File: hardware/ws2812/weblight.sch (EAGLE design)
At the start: 16 parts, among them U1 ATtiny85-20SU

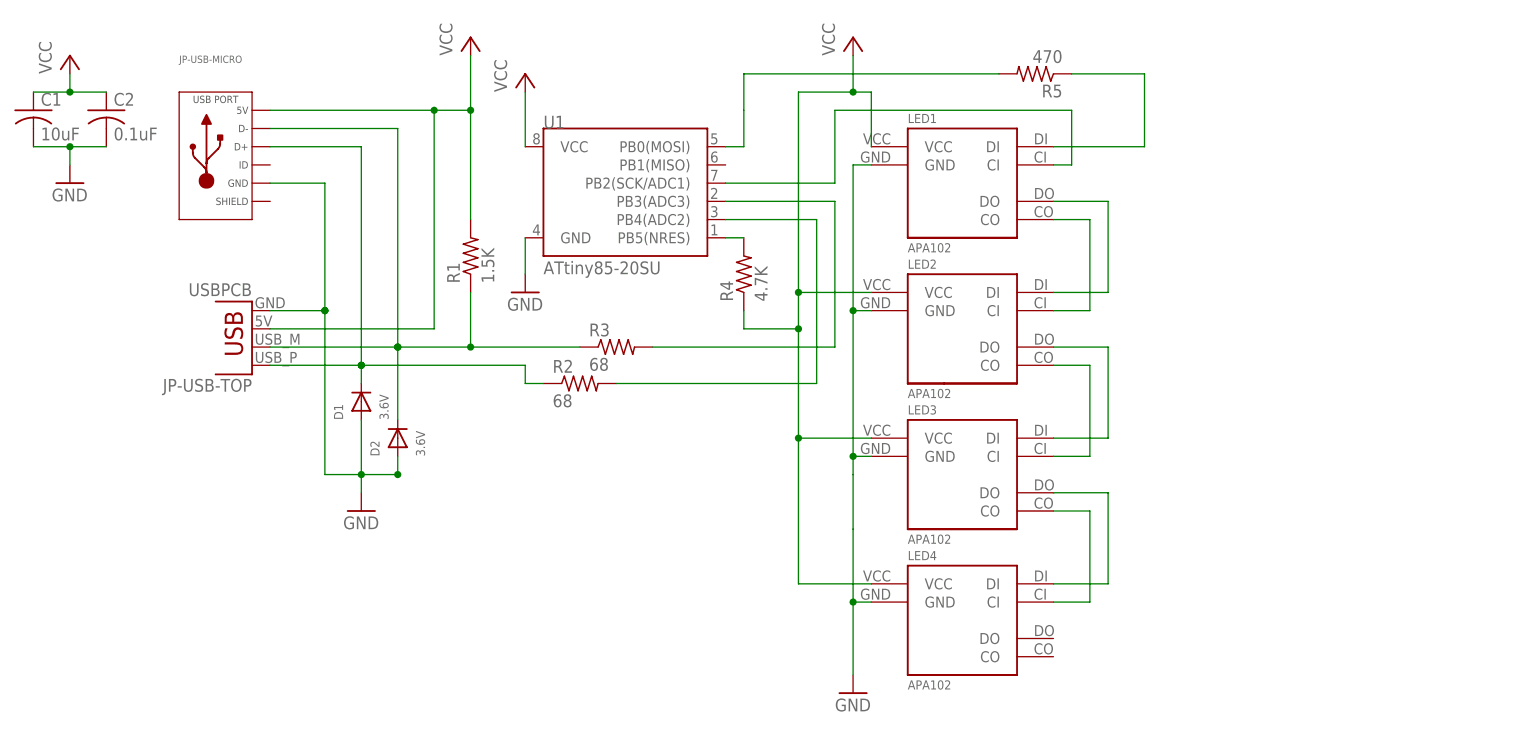
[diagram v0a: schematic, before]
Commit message: Separate LED type and adopt new board versioning scheme
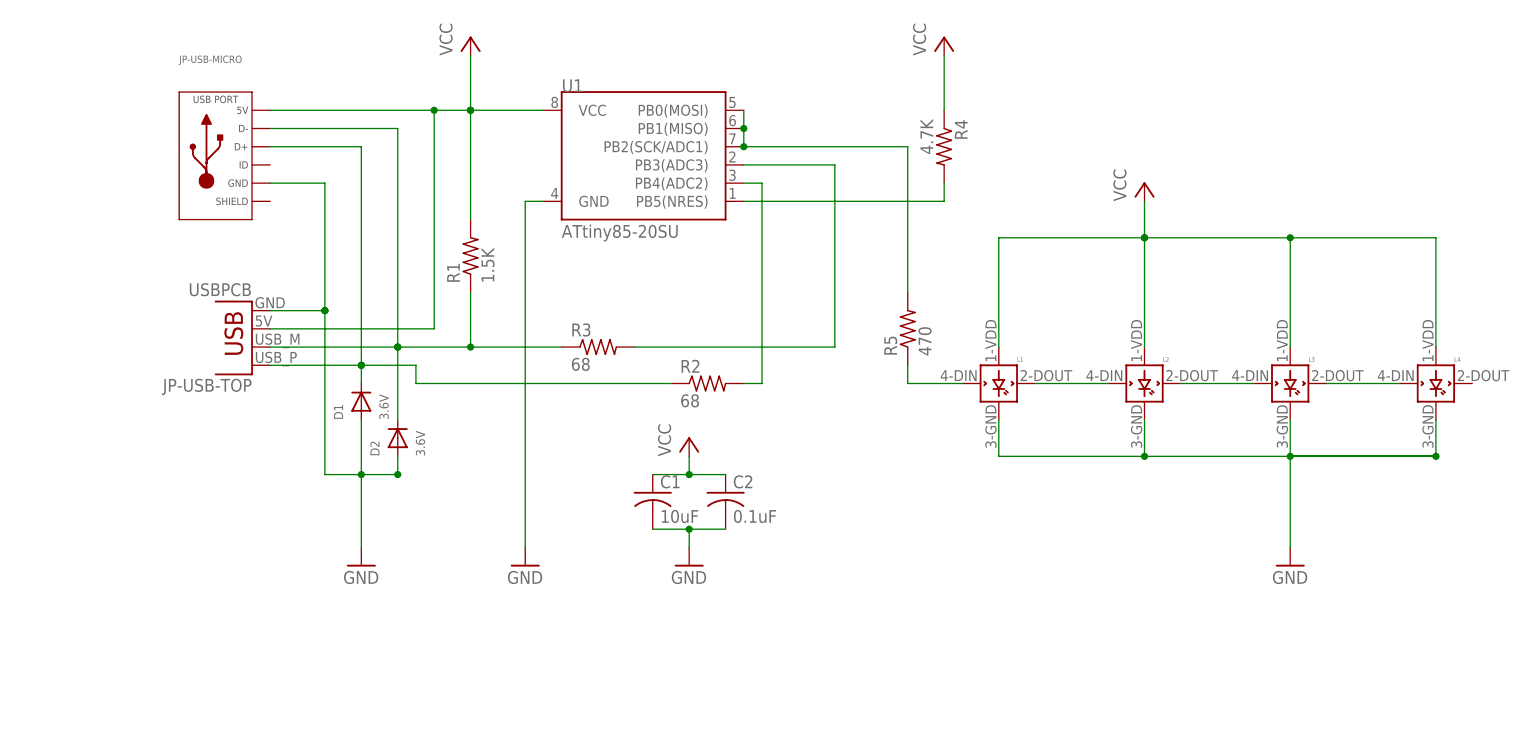
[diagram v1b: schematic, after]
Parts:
- removed LED1, LED2, LED3, LED4: APA102, weblight:APA102
- added L1, L2, L3, L4: WS2812B, weblight:WS2812B
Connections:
- removed net CLK_1: LED1.CI, U1.PB2(SCK/ADC1)
- removed net CLK_2: LED1.CO, LED2.CI
- removed net CLK_3: LED2.CO, LED3.CI
- removed net CLK_4: LED3.CO, LED4.CI
- net DIN_1: now also L1.DIN; no longer LED1.DI
- net DIN_2: now also L1.DOUT, L2.DIN; no longer LED1.DO, LED2.DI
- net DIN_3: now also L2.DOUT, L3.DIN; no longer LED2.DO, LED3.DI
- net DIN_4: now also L3.DOUT, L4.DIN; no longer LED3.DO, LED4.DI
- net DIN_RAW: now also U1.PB1(MISO), U1.PB2(SCK/ADC1)
- net GND: now also L1.GND, L2.GND, L3.GND, L4.GND; no longer LED1.GND, LED2.GND, LED3.GND, LED4.GND
- net VCC: now also L1.VDD, L2.VDD, L3.VDD, L4.VDD; no longer LED1.VCC, LED2.VCC, LED3.VCC, LED4.VCC
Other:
- moved on the sheet: C1, C2, R2, R3, R4, R5, U1
